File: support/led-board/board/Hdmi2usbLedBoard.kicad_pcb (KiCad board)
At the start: 2 copper layers, 29.5 x 31.5 mm, 35 parts, among them P1 CONN_20X2, Q1 OPTO_NPN

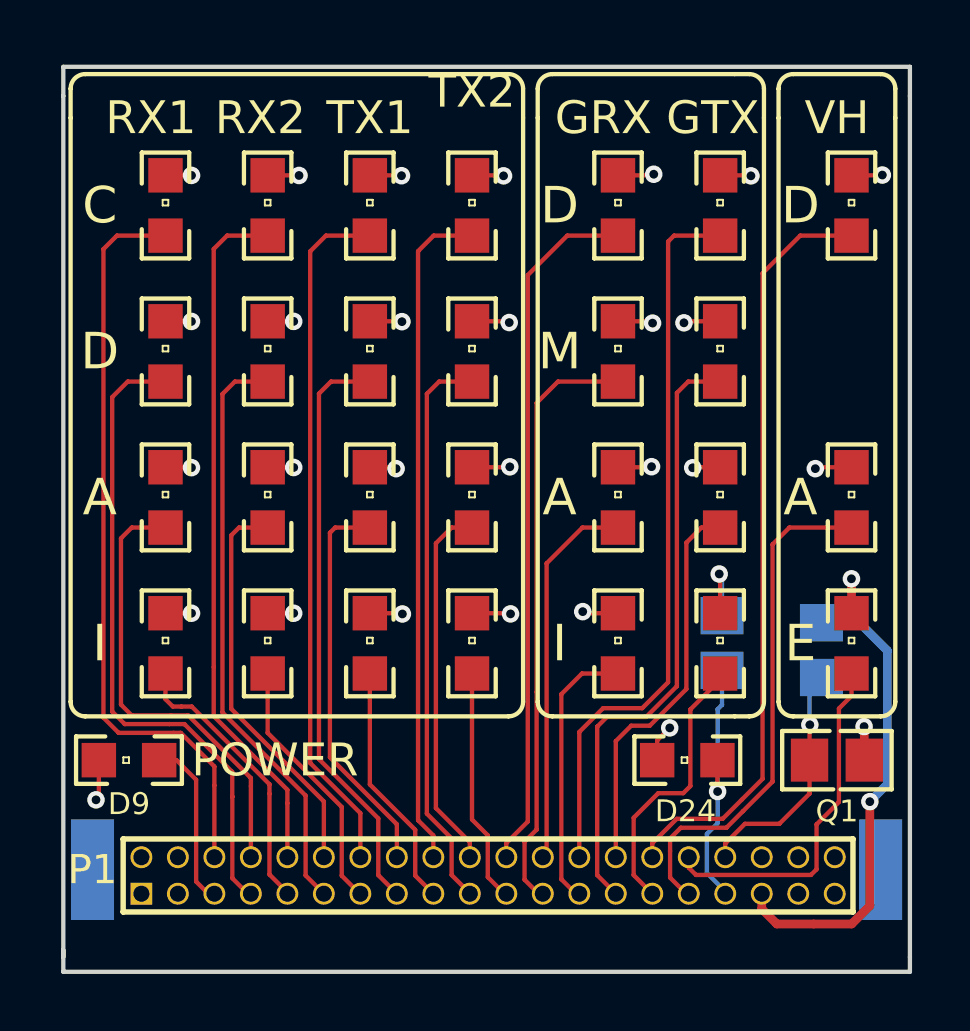
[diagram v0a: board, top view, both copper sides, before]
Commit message: Issue #1117 - LED board for HDMI
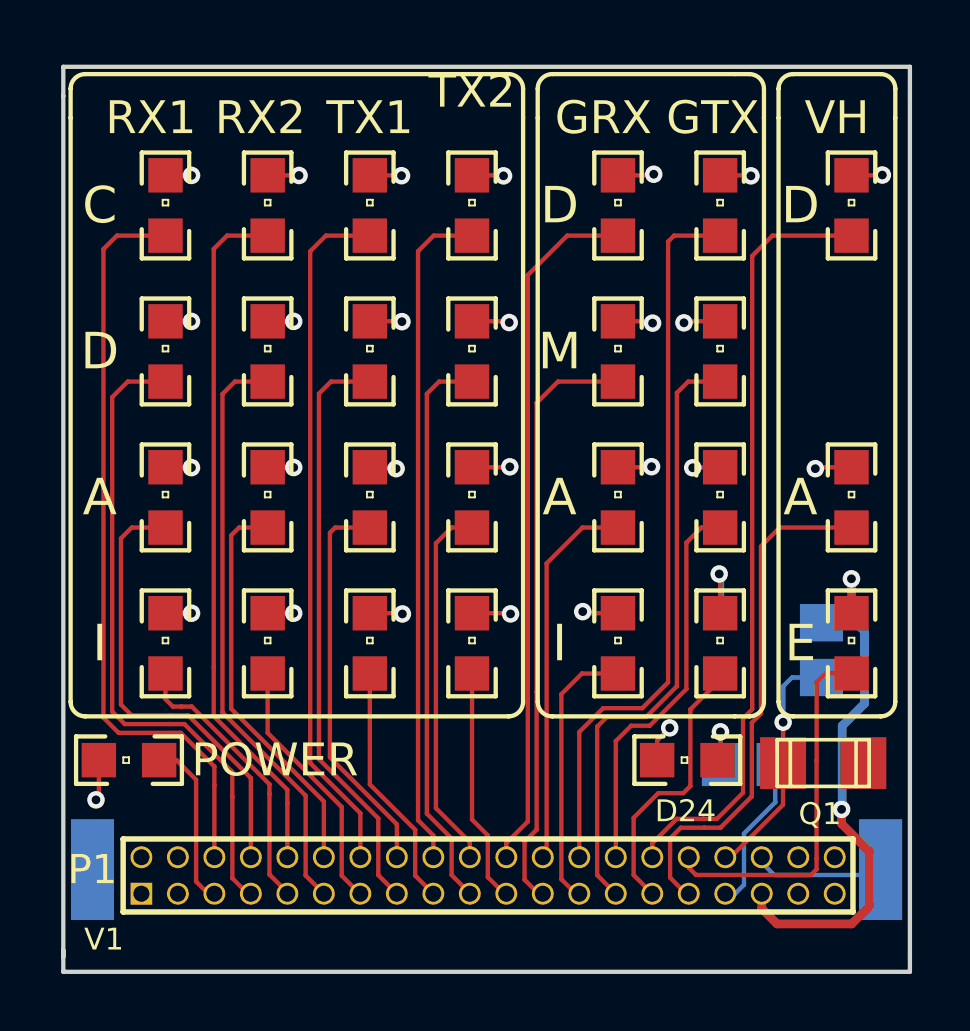
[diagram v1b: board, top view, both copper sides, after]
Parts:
- Q1: footprint c_0805 -> c_1206
- R2: value 2.2K -> 1K
- moved R2 4.32 mm to (155.9, 80.4), turned to 180 degrees
- moved Q1 0.49 mm to (158.5, 80.4)
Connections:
- D24 pad 1: /LED-IR -> N-0000012
- R2 pad 1: GND -> N-0000012
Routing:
- net /LED-IR: track 9.35 -> 5.42 mm, vias 1 -> 0
- net GND: track 36.3 -> 39.7 mm, vias 30 -> 29
- net N-0000012: track 0.00 -> 2.17 mm, vias 0 -> 1
- net /LED-V-E: track 12.3 -> 12.8 mm
- net /IR SENSE: track 7.84 -> 8.35 mm
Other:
- rule trace_min: 0.1524 -> 0.006
- rule via_min_size: 0.6096 -> 0.024
- board text added: "V1"
